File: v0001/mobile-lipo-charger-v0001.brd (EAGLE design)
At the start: 82.9 x 96.2 mm, 74 parts, among them IC1 AD8610MR, IC3 AD8610MR, IC5 STM32F429NGH, SW2 DHT-4235A, U3 3.3V, U4 3.3V

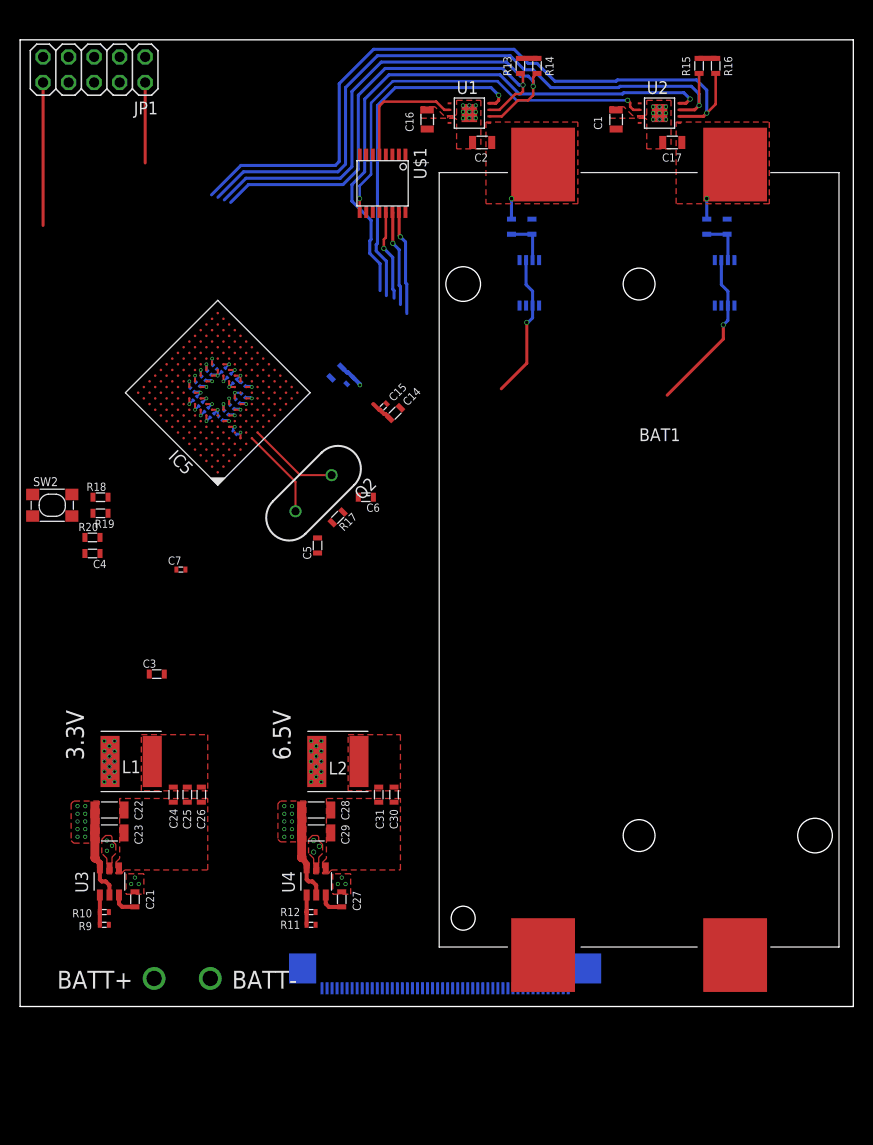
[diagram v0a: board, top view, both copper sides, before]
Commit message: Routed
Routed new chip
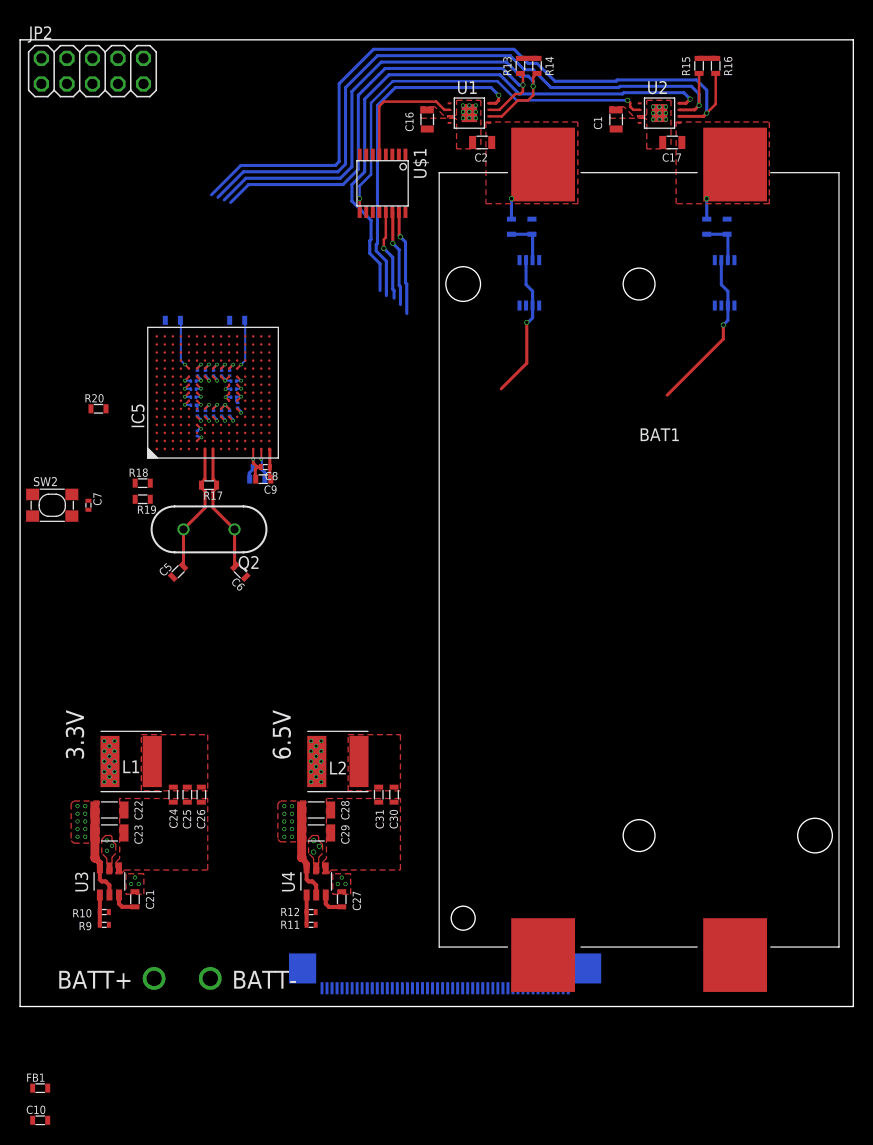
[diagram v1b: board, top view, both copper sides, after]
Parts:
- removed C12, C14: 1u, common:0603L3
- removed C13, C15: 100n, common:0402L3
- removed JP1: (no value), pinhead:2X05
- added C10, C18, C9: 1u, common:0603L3
- added C11, C8: 100n, common:0402L3
- added FB1: (no value), common:0603L3
- added JP2: (no value), pinhead:2X05
- moved C3 36.1 mm to (21.6, 79.2), flipped to the bottom
- moved C4 24.5 mm to (15.2, 79.2), flipped to the bottom, turned to 0 degrees
- moved C6 14.5 mm to (21.9, 54.2), turned to 135 degrees
- moved C5 14.1 mm to (15.7, 54.2), turned to 45 degrees
- moved R17 13.2 mm to (18.8, 62.8), turned to 180 degrees
- moved R20 12.8 mm to (7.80, 70.4)
- moved C7 11.2 mm to (6.80, 60.8), turned to 270 degrees
- moved Q2 11.0 mm to (18.8, 58.4), turned to 180 degrees
- moved R18 4.43 mm to (12.2, 63.0)
- moved R19 4.43 mm to (12.2, 61.4)
- moved C50 3.72 mm to (17.6, 68.0), turned to 90 degrees
- moved C45 2.36 mm to (17.6, 70.0), turned to 270 degrees
- moved C41 2.23 mm to (20.8, 70.0), turned to 270 degrees
- moved C40 2.17 mm to (21.6, 70.8), turned to 90 degrees
- moved C46 2.11 mm to (17.2, 70.8), turned to 0 degrees
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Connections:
- net N$6 renamed OSC_IN
- net N$7 renamed OSC_OUT
- removed net N$15: C14.P$1, C15.P$1
- removed net VBAT: IC5.C1
- removed net VREF+: IC5.P1
- removed net VREF-: IC5.N1
- new net N$3: IC5.J1, R18.P$2
- net GND: now also C10.P$2, C11.P$2, C18.P$2, C8.P$2, C9.P$2, IC5.L5, IC5.N1, JP2.3, JP2.5, JP2.9; no longer C12.P$2, C13.P$2, C14.P$2, C15.P$2, JP1.3, JP1.5, JP1.9
- net RST: now also JP2.10; no longer IC5.J1, JP1.10, R18.P$2
- net TCK_SWCLK: now also JP2.4; no longer JP1.4
- net TMS_SWDIO: now also JP2.2; no longer JP1.2
- net VDD: now also C10.P$1, FB1.P$1, IC5.C1, IC5.E5, JP2.1; no longer C12.P$1, C13.P$1, JP1.1
- net VDDA: now also C11.P$1, C18.P$1, C8.P$1, C9.P$1, FB1.P$2, IC5.P1
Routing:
- net RST: track 14.2 -> 0.00 mm
- net TMS_SWDIO: track 8.00 -> 0.00 mm
- net VDDA: track 0.00 -> 6.25 mm, vias 0 -> 1
- net GND: track 20.5 -> 26.6 mm, vias 32 -> 33
- net VCAP2: track 0.00 -> 5.15 mm, vias 0 -> 1
- net VCAP1: track 0.00 -> 5.15 mm, vias 0 -> 1
- net OSC_IN: track 9.07 -> 12.9 mm
- net OSC_OUT: track 9.13 -> 12.9 mm
- net VDD: track 28.8 -> 26.1 mm, vias 19 -> 18
- net N$15: track 2.31 -> 0.00 mm

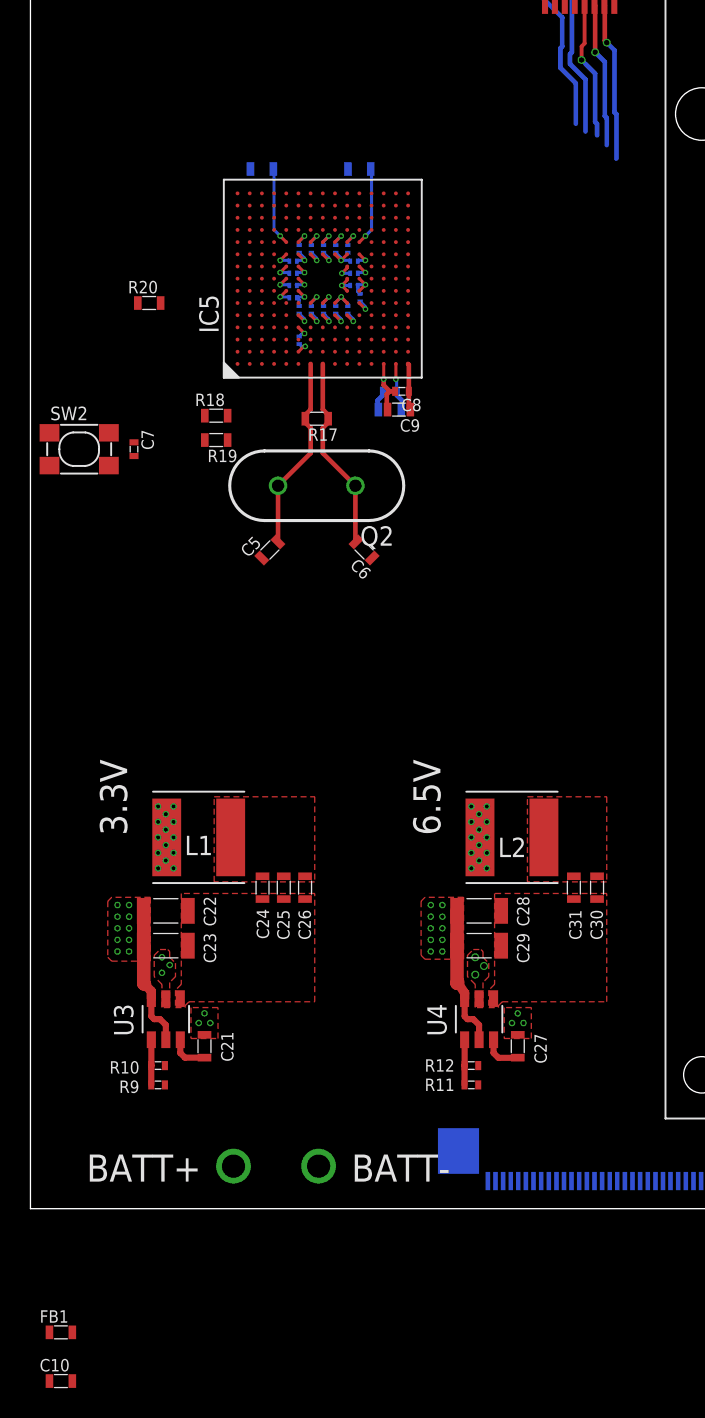
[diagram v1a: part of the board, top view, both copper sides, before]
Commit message: Routed ferrite bead
Routed the ferrite bead for VDDA and VREF+
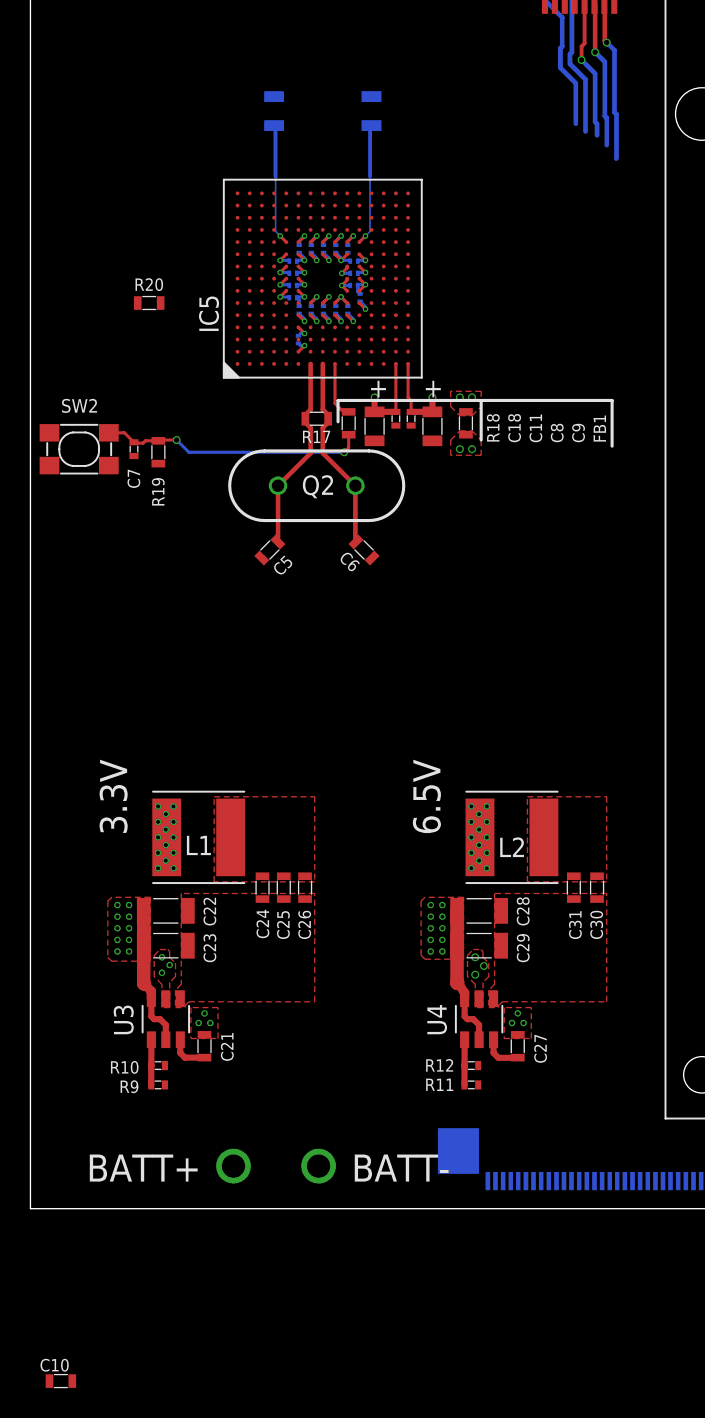
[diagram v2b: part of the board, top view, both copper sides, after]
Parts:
- C18, C3, C4, C9: device common:0603L3 -> common:0805L3
- moved FB1 65.4 mm to (28.6, 62.5), turned to 90 degrees
- moved R18 8.71 mm to (20.9, 62.5), turned to 90 degrees
- moved R19 3.88 mm to (8.40, 60.6), turned to 90 degrees
- moved C4 3.88 mm to (16.0, 83.0), turned to 90 degrees
- moved C3 3.88 mm to (22.4, 83.0), turned to 90 degrees
- moved C9 2.46 mm to (26.4, 62.3), turned to 270 degrees
- moved C8 1.90 mm to (25.0, 62.8), turned to 270 degrees
- moved C11 1.84 mm to (24.0, 62.8), flipped to the top, turned to 270 degrees
- moved C18 1.49 mm to (22.6, 62.3), flipped to the top, turned to 270 degrees
- moved C50 0.07 mm to (17.6, 68.0)
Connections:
- net GND: now also C18.2, C3.2, C4.2, C9.2; no longer C18.P$2, C3.P$2, C4.P$2, C9.P$2
- net VCAP1: now also C3.1; no longer C3.P$1
- net VCAP2: now also C4.1; no longer C4.P$1
- net VDDA: now also C18.1, C9.1; no longer C18.P$1, C9.P$1
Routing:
- net RST_BUTTON: track 0.00 -> 17.4 mm, vias 0 -> 2
- net GND: track 26.6 -> 20.7 mm, vias 33 -> 32
- net VDDA: track 6.25 -> 11.1 mm, vias 1 -> 4
- net N$3: track 0.00 -> 3.77 mm
- net VCAP1: track 5.15 -> 7.98 mm
- net VCAP2: track 5.15 -> 7.98 mm
- net VDD: vias 18 -> 20
- added copper zone on layer 1, net VDDA
- added copper zone on layer 2, net VDDA
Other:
- board text added: "+"

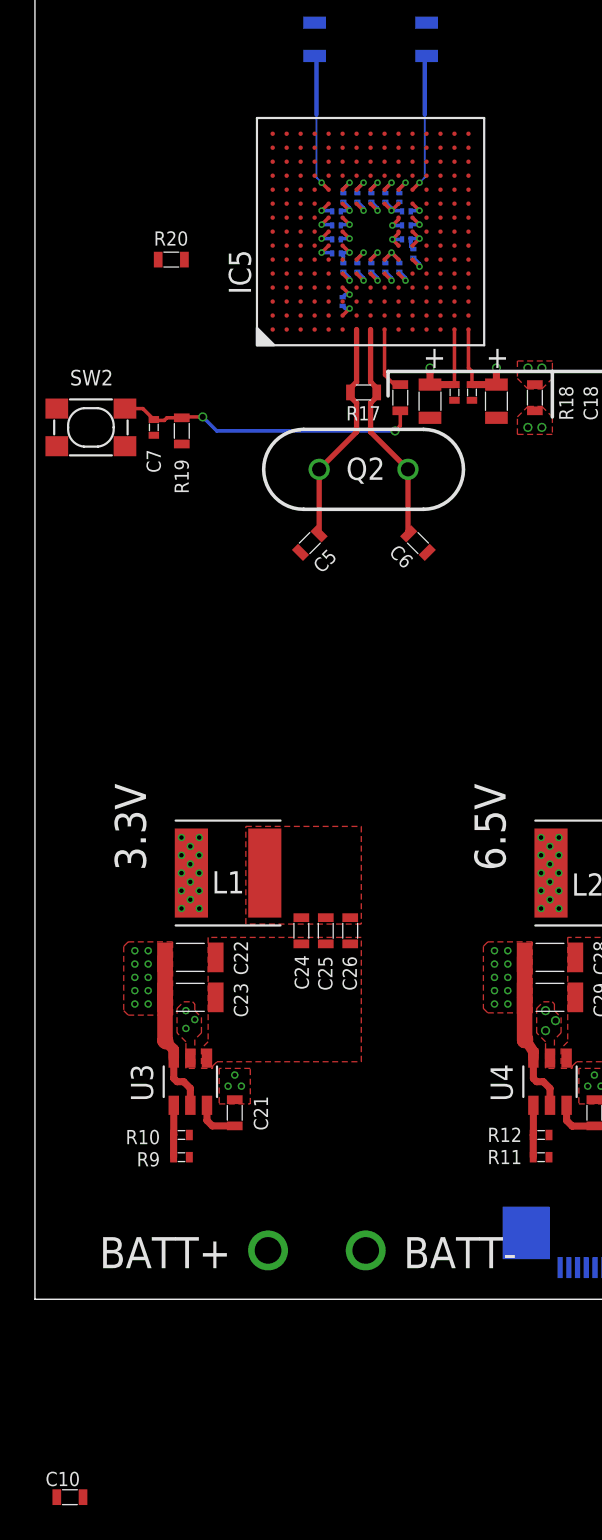
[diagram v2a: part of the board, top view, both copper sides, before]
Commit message: Routing
Began routing TFT signals
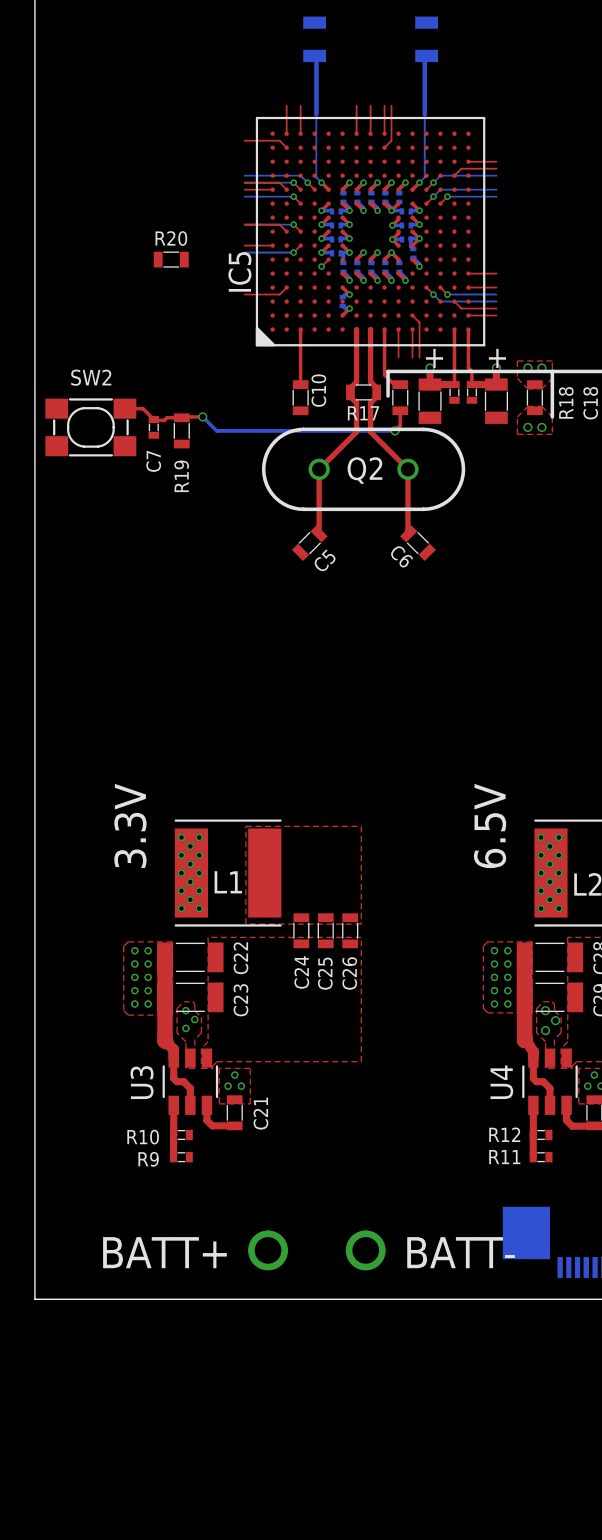
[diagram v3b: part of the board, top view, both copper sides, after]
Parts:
- moved C10 64.3 mm to (15.2, 62.5), turned to 270 degrees
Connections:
- removed net TFT_CS#: J1.38
- removed net TFT_DB0: J1.32
- removed net TFT_DB1: J1.31
- removed net TFT_DB10: J1.22
- removed net TFT_DB11: J1.21
- removed net TFT_DB12: J1.20
- removed net TFT_DB13: J1.19
- removed net TFT_DB14: J1.18
- removed net TFT_DB15: J1.17
- removed net TFT_DB16: J1.16
- removed net TFT_DB17: J1.15
- removed net TFT_DB2: J1.30
- removed net TFT_DB3: J1.29
- removed net TFT_DB4: J1.28
- removed net TFT_DB5: J1.27
- removed net TFT_DB6: J1.26
- removed net TFT_DB7: J1.25
- removed net TFT_DB8: J1.24
- removed net TFT_DB9: J1.23
- removed net TFT_DE: J1.14
- removed net TFT_DOTCLK: J1.13
- removed net TFT_HSYNC: J1.12
- removed net TFT_IM0: J1.6
- removed net TFT_IM1: J1.7
- removed net TFT_IM2: J1.8
- removed net TFT_IM3: J1.9
- removed net TFT_RESET#: J1.10
- removed net TFT_RS_SCL: J1.37
- removed net TFT_SDI: J1.34
- removed net TFT_TE: J1.39
- removed net TFT_VSYNC: J1.11
- new net B2: IC5.B11, J1.32
- new net B3: IC5.B8, J1.31
- new net B4: IC5.C7, J1.30
- new net B5: IC5.R2, J1.29
- new net B6: IC5.A7, J1.28
- new net B7: IC5.B4, J1.27
- new net CSX: IC5.M4, J1.38
- new net DCX_SCL: IC5.K1, J1.37
- new net DOTCLK: IC5.J14, J1.13
- new net ENABLE: IC5.L1, J1.14
- new net G2: IC5.P3, J1.26
- new net G3: IC5.C8, J1.25
- new net G4: IC5.P12, J1.24
- new net G5: IC5.R13, J1.23
- new net G6: IC5.G15, J1.22
- new net G7: IC5.C11, J1.21
- new net HSYNC: IC5.H15, J1.12
- new net IM0: IC5.D12, J1.6
- new net IM1: IC5.D11, J1.7
- new net IM2: IC5.C10, J1.8
- new net IM3: IC5.A11, J1.9
- new net R2: IC5.B14, J1.20
- new net R3: IC5.R5, J1.19
- new net R4: IC5.C15, J1.18
- new net R5: IC5.B15, J1.17
- new net R6: IC5.R4, J1.16
- new net R7: IC5.J15, J1.15
- new net RDX: IC5.M10
- new net SDA: IC5.L2, J1.34
- new net TE: IC5.N10, J1.39
- new net VSYNC: IC5.N4, J1.11
- new net WRX_DCX: IC5.M11
- net RST: now also J1.10
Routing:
- net RDX: track 0.00 -> 4.33 mm, vias 0 -> 1
- net WRX_DCX: track 0.00 -> 4.33 mm, vias 0 -> 1
- net IM1: track 0.00 -> 4.33 mm, vias 0 -> 1
- net CSX: track 0.00 -> 4.33 mm, vias 0 -> 1
- net IM2: track 0.00 -> 3.37 mm, vias 0 -> 1
- net G3: track 0.00 -> 3.37 mm, vias 0 -> 1
- net B4: track 0.00 -> 3.37 mm, vias 0 -> 1
- net TE: track 0.00 -> 3.37 mm, vias 0 -> 1
- net G7: track 0.00 -> 3.37 mm, vias 0 -> 1
- net VSYNC: track 0.00 -> 3.37 mm, vias 0 -> 1
- net VDD: track 26.1 -> 29.3 mm
- net R2: track 0.00 -> 2.57 mm
- net B3: track 0.00 -> 2.57 mm
- net SDA: track 0.00 -> 2.57 mm
- net G2: track 0.00 -> 2.57 mm
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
